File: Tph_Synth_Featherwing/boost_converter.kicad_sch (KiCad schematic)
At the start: 11 parts, among them U1 PAM2401SCADJ

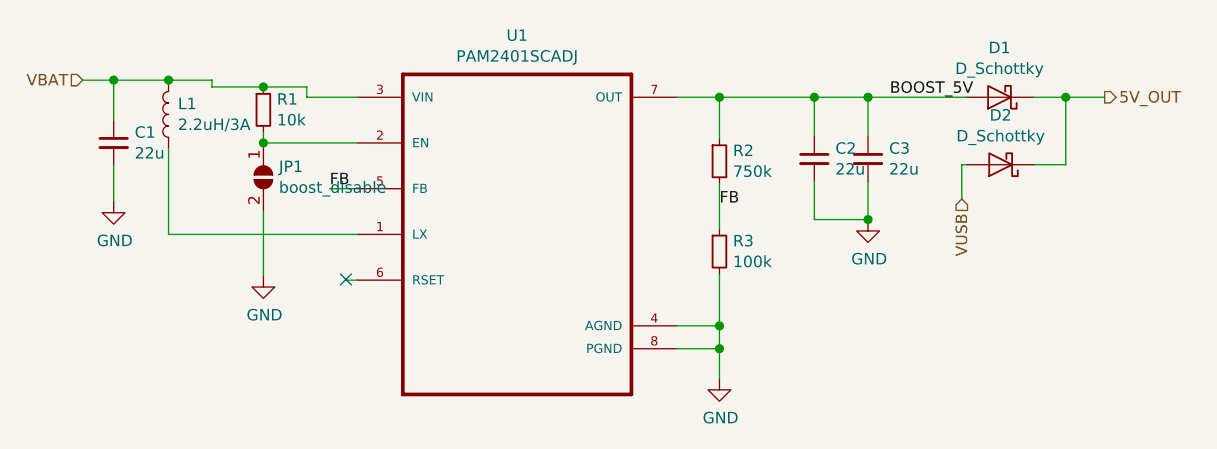
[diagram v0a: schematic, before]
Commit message: Upgrade design to KiCad 10; clear ERC and DRC violations
Co-authored-by: Copilot <223556219+Copilot@users.noreply.github.com>
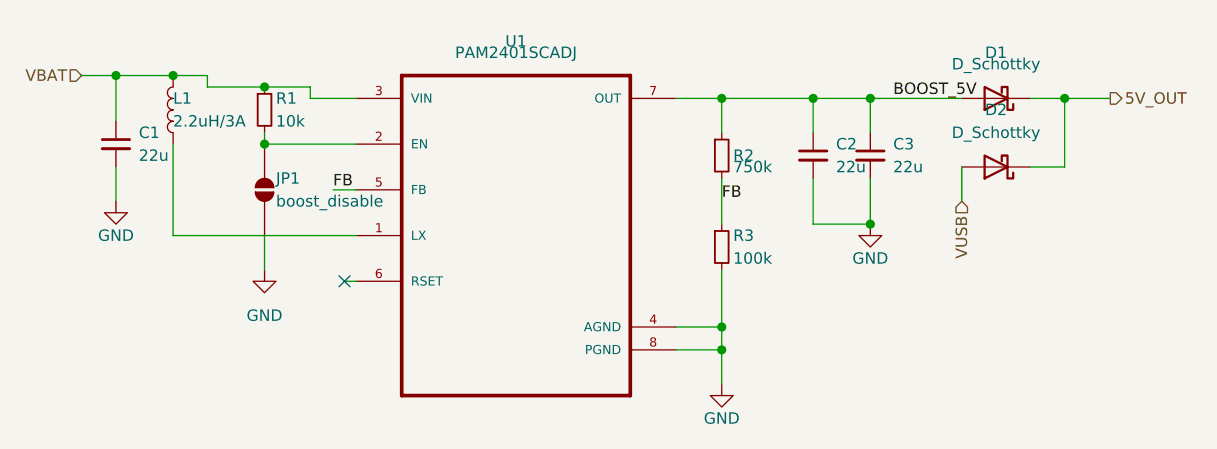
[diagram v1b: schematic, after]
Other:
- moved on the sheet: D2, L1, R2, R3

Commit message: Release v0.4 with complete KiCad 10 schematic-PCB parity
Synchronize pad nets, schematic paths, component fields and BOM exclusions while retaining routing and placement. Restore project-local STEP models, fix edge silkscreen using local footprint variants, update revision metadata and improve schematic readability. Include inspected PDF and PCB renders.

Co-authored-by: Copilot <223556219+Copilot@users.noreply.github.com>
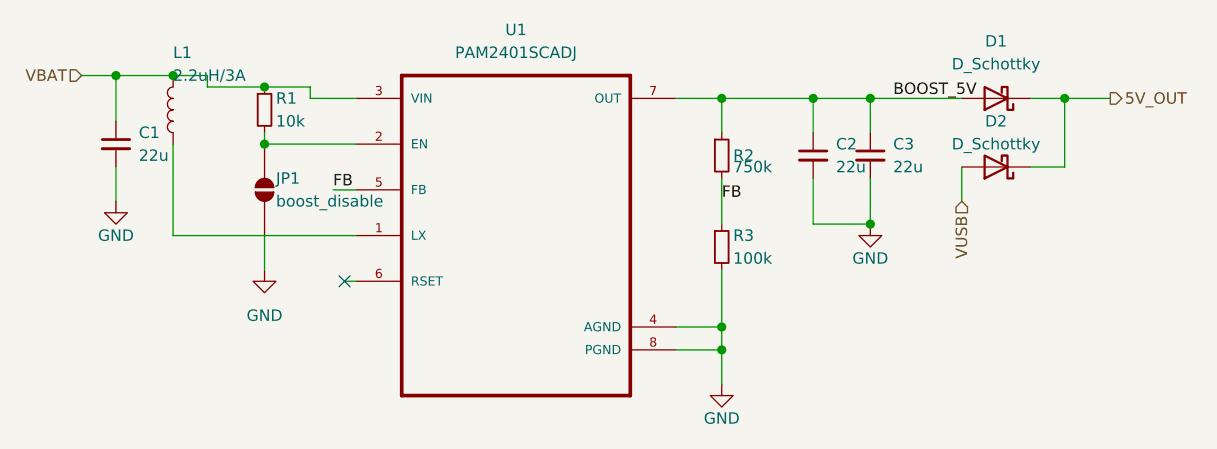
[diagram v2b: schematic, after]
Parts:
- JP1: now left out of the parts list
- L1: footprint Inductor_SMD:L_Bourns-SRR1005 -> FeatherWing_v04:L_Bourns-SRR1005_ProjectModel
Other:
- title: (none) -> 3-Phase Synth FeatherWing
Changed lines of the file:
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@@
 	(generator_version "10.0")
 	(paper "A4")
+	(title_block
+		(title "3-Phase Synth FeatherWing")
+		(date "2026-10-28")
+		(rev "0.4")
+	)
 	(junction
 		(at 175.26 67.31)
@@
 		(dnp no)
 		(property "Reference" "U1"
-			(at 142.24 60.96 0)
+			(at 142.24 59.69 0)
 			(show_name no)
 			(do_not_autoplace no)
@@
 		(dnp no)
 		(property "Reference" "L1"
-			(at 104.14 67.31 0)
+			(at 104.14 62.23 0)
 			(show_name no)
 			(do_not_autoplace no)
@@
 		)
 		(property "Value" "2.2uH/3A"
-			(at 104.14 69.85 0)
+			(at 104.14 64.77 0)
 			(show_name no)
 			(do_not_autoplace no)
@@
 			)
 		)
-		(property "Footprint" "Inductor_SMD:L_Bourns-SRR1005"
+		(property "Footprint" "FeatherWing_v04:L_Bourns-SRR1005_ProjectModel"
 			(at 104.14 68.58 0)
 			(hide yes)
@@
 		(dnp no)
 		(property "Reference" "D1"
-			(at 195.58 62.23 0)
+			(at 195.58 60.96 0)
 			(show_name no)
 			(do_not_autoplace no)
@@
 		(body_style 1)
 		(exclude_from_sim no)
-		(in_bom yes)
+		(in_bom no)
 		(on_board yes)
 		(in_pos_files yes)
@@
 		(dnp no)
 		(property "Reference" "D2"
-			(at 195.58 68.58 0)
+			(at 195.58 69.85 0)
 			(show_name no)
 			(do_not_autoplace no)
@@
 		)
 		(property "Value" "D_Schottky"
-			(at 195.58 71.12 0)
+			(at 195.58 72.39 0)
 			(show_name no)
 			(do_not_autoplace no)
